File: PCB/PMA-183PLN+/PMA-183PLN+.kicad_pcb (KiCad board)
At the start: 4 copper layers, 55.3 x 35 mm, 25 parts, among them J1 Conn_Coaxial, J2 Conn_Coaxial, U1 PMA-183PLN+, U2 MIC5219-2.6YM5-TR

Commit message: PMA-183PLN+ schematic pdf added and title text fixed
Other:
- board text added: "6000-18000 MHz SMT LNA"
- board text removed: "50-10000 MHz SMT LNA"
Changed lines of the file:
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@@
     (effects (font (size 1.5 1.5) (thickness 0.3) bold) (justify left))
   )
-  (gr_text "50-10000 MHz SMT LNA" (at 169.5 195.5) (layer "Cmts.User")
+  (gr_text "6000-18000 MHz SMT LNA" (at 169.5 195.5) (layer "Cmts.User")
     (effects (font (size 1.5 1.5) (thickness 0.3) bold) (justify left))
   )

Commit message: Updated silkscreen and reference designators on EMS boards
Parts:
- moved C8 0.06 mm to (138.5, 77.6)
- moved U2 0.06 mm to (135.1, 76.2)
- renumbered TP3 to 2.6VDC, TP1 to GND, J1 to RF-In, J2 to RF-Out, TP2 to Vin
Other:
- board text added: "PMA-183PLN+"
- board text added: "RF-EMS"
- board text removed: "Designed By: Remy Nguyen"
- board text removed: "RF-DFS"

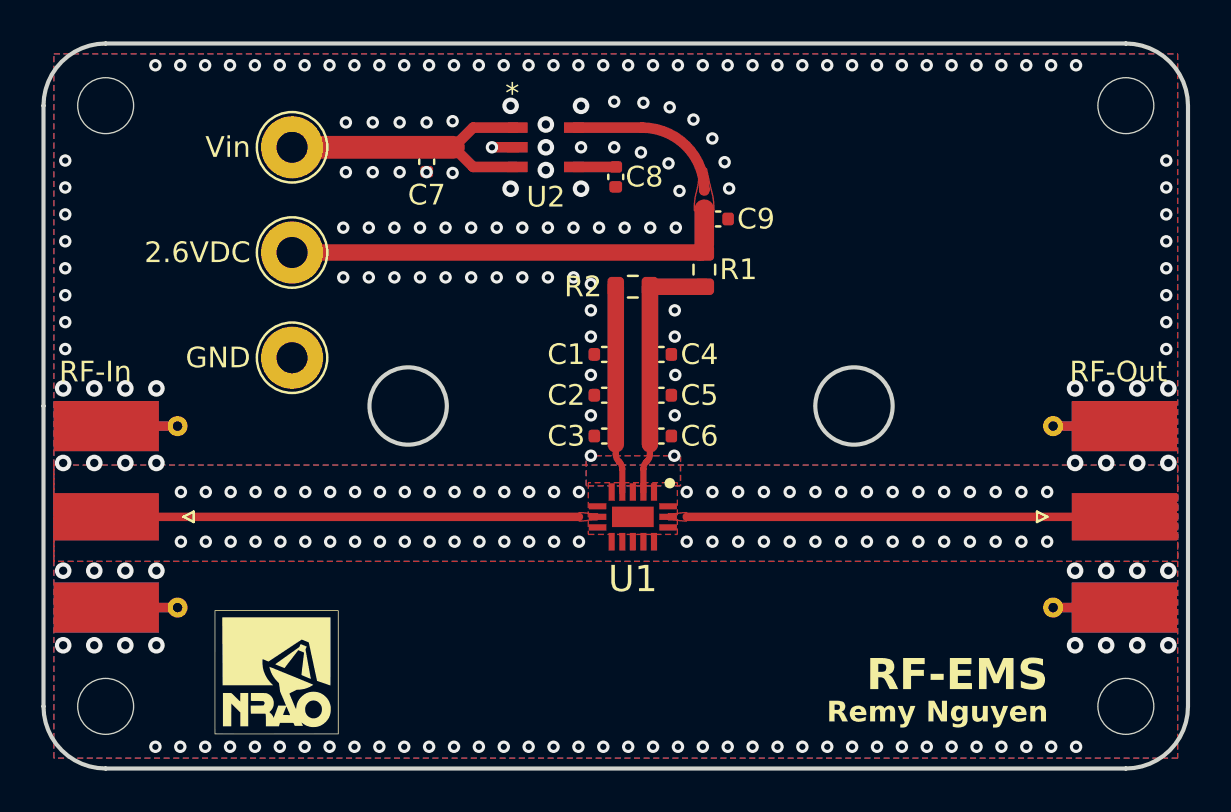
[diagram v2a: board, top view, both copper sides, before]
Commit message: PMA-183PLN+ PCB Rev A completed
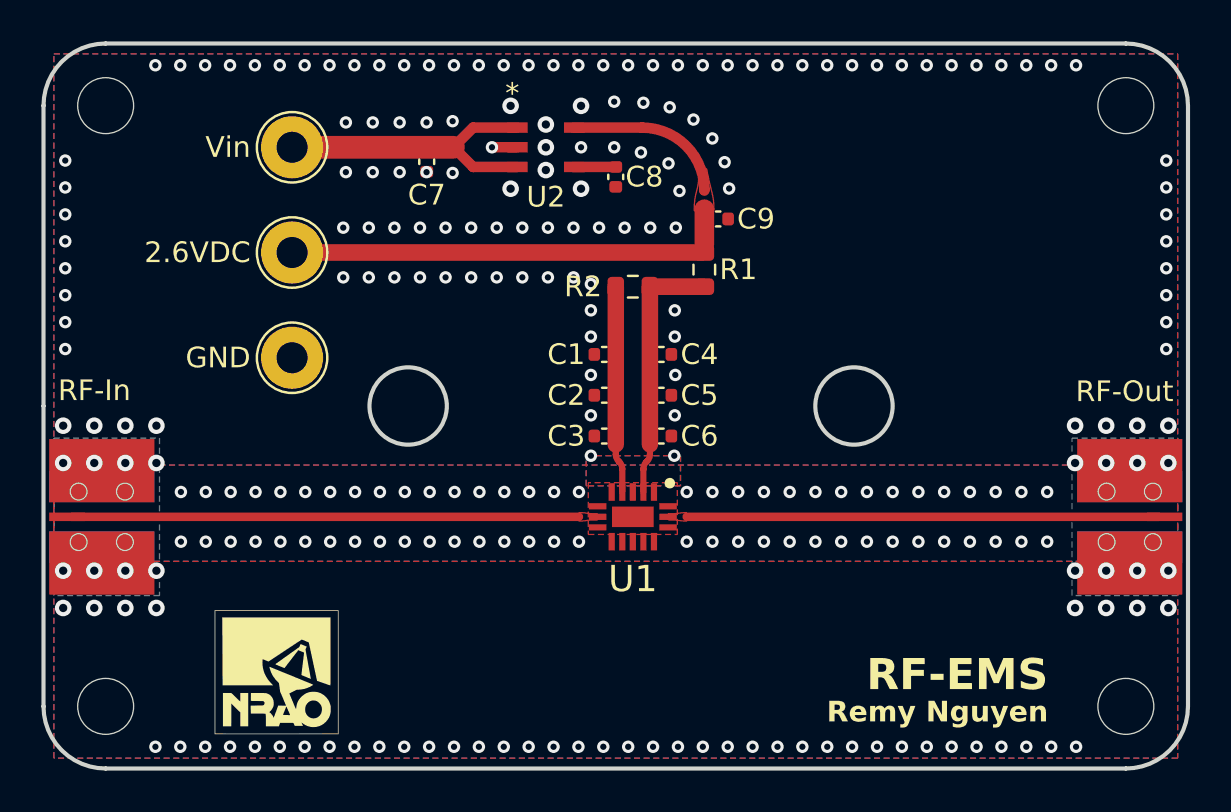
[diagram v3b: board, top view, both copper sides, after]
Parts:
- removed ?: , imports:RF-DFS-GCPW-OSH
- added  : LOGO, footprints.pretty:GCPW_osh2_90mm_user, F.Cu at (207.0, 147.5)
- RF-In, RF-Out: footprint footprints:SMA_Molex_73251-1153_EdgeMount_Horizontal_TunedOSH -> footprints:Mueller BU-1420761881
- moved RF-Out 0.25 mm to (161.6, 94.0)
- moved RF-In 0.21 mm to (115.4, 94.0)
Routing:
- net Net-(IC2-RF-OUT): track 21.1 -> 22.8 mm
- net Net-(IC2-RF-IN): track 22.8 -> 24.5 mm
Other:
- board text added: "Hole pattern for Hammond 1554B"

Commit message: PMA-183PLN+ Rev B complete
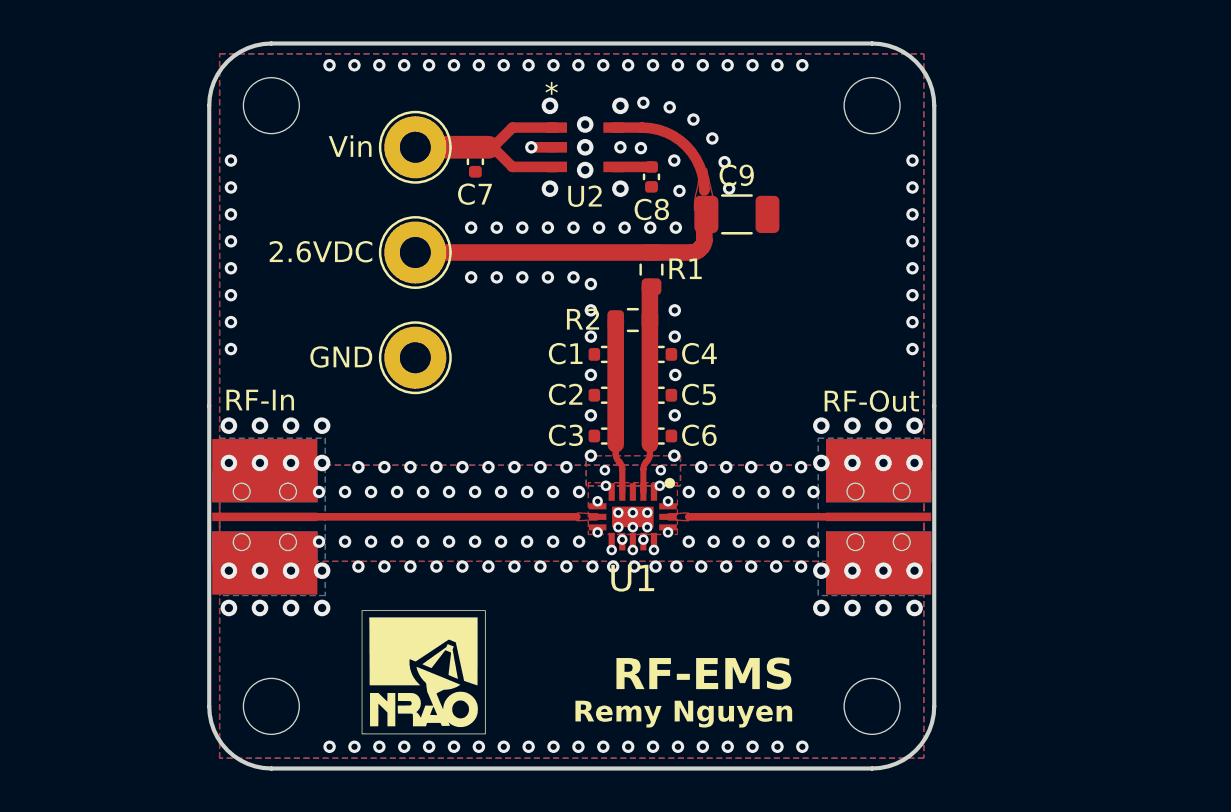
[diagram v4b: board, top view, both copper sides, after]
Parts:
- removed the   at (207.0, 147.5)
- added  : LOGO, footprints.pretty:GCPW_osh3_90mm_user, F.Cu at (207.0, 147.5)
- C9: footprint Capacitor_SMD:C_0402_1005Metric -> Capacitor_SMD:C_1206_3216Metric
- moved REF** 12.2 mm to (150.8, 103.2)
- moved REF** 12.2 mm to (150.8, 74.2)
- moved RF-Out 12.2 mm to (149.3, 94.0)
- moved REF** 8.00 mm to (121.8, 74.2)
- moved REF** 8.00 mm to (121.8, 103.2)
- moved RF-In 8.00 mm to (123.4, 94.0)
- moved G*** 7.10 mm to (129.2, 101.5)
- moved 2.6VDC 5.95 mm to (128.8, 81.2)
- moved GND 5.95 mm to (128.8, 86.3)
- moved Vin 5.95 mm to (128.8, 76.2)
- moved R1 2.55 mm to (140.2, 82.1)
- moved C7 2.35 mm to (131.7, 76.9)
- moved U2 1.90 mm to (137.0, 76.2)
- moved C8 1.72 mm to (140.2, 77.6)
- moved R2 1.61 mm to (139.3, 84.5)
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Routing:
- net Net-(IC2-RF-OUT): track 22.8 -> 10.8 mm
- net Net-(IC2-RF-IN): track 24.5 -> 15.1 mm
- net 2.6VDC: track 29.7 -> 21.8 mm
- net Vin: track 14.7 -> 10.4 mm
- net Net-(IC2-VDD): track 12.6 -> 9.99 mm
- net Net-(IC2-VE): track 9.99 -> 8.38 mm
- net GND: vias 253 -> 217
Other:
- board size 55.3 x 35 mm -> 35 x 35 mm
- board text added: "7/8/2024"
- board text added: "B"
- board text added: "Rev B"
- board text removed: "4/12/2024"
- board text removed: "A"
- board text removed: "Hole pattern for Hammond 1554B"
